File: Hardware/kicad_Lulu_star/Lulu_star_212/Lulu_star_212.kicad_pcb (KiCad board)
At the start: 2 copper layers, 16.7 x 14.9 mm, 8 parts, among them J1 Conn_01x03_Female, P1 Soldering_pad, Q1 Q_NMOS_GSD, T1 Q_NPN_BEC

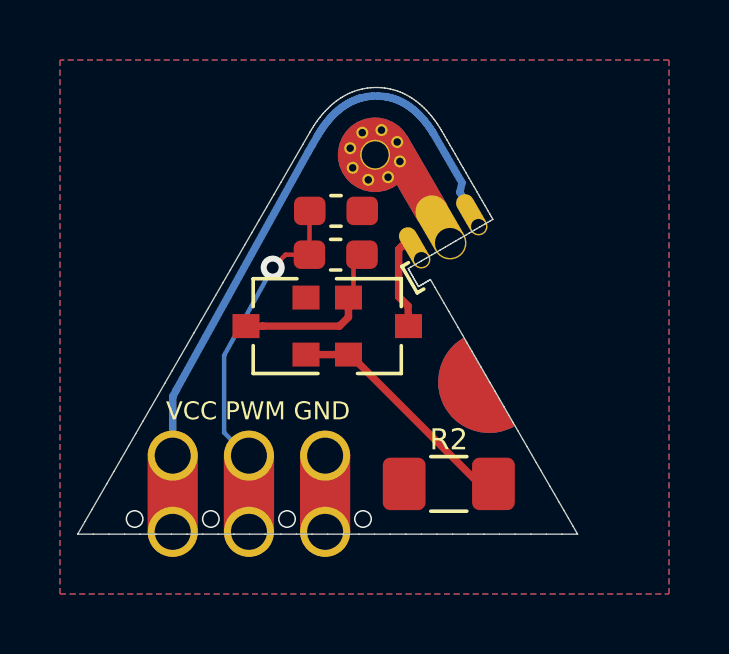
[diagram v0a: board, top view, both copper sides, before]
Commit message: Move down all components of the PCB
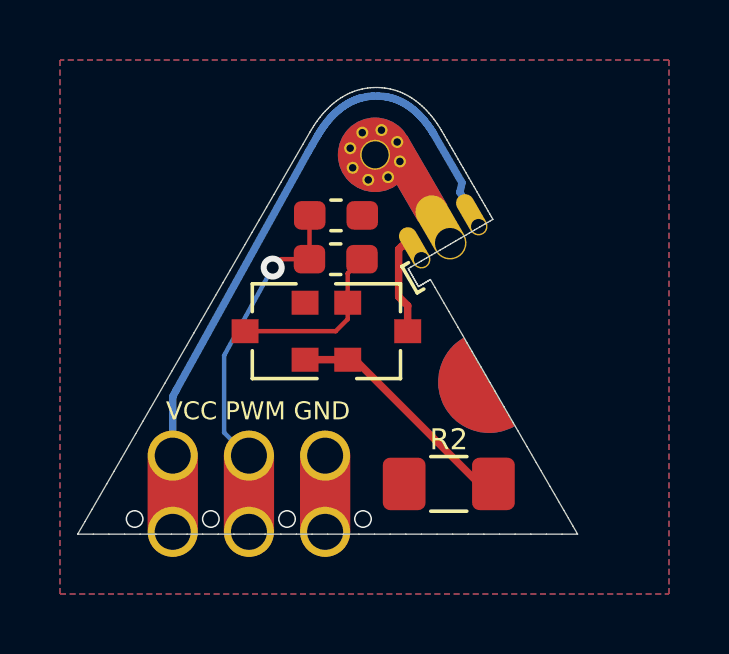
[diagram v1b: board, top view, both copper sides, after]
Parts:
- moved T1 0.17 mm to (68.8, 38.3)
- moved Q1 0.17 mm to (72.2, 38.3)
- moved R1 0.15 mm to (70.8, 35.9)
- moved R3 0.15 mm to (70.8, 34.5)
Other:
- net class Default: clearance 0.15 -> 0.2
- net class POWER: clearance 0.15 -> 0.2
- net class SIG: clearance 0.15 -> 0.2
- rule trace_clearance: 0.15 -> 0.2
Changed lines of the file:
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@@
     (thickness 1)
     (drawings 292)
-    (tracks 97)
+    (tracks 95)
     (zones 0)
     (modules 8)
@@
   (setup
     (last_trace_width 0.25)
-    (trace_clearance 0.15)
+    (trace_clearance 0.2)
     (zone_clearance 0.12)
     (zone_45_only yes)
@@
   (net 6 +3V3)
   (net_class Default "This is the default net class."
-    (clearance 0.15)
+    (clearance 0.2)
     (trace_width 0.25)
     (via_dia 0.8)
@@
   )
   (net_class POWER ""
-    (clearance 0.15)
+    (clearance 0.2)
     (trace_width 0.25)
     (via_dia 0.8)
@@
   )
   (net_class SIG ""
-    (clearance 0.15)
+    (clearance 0.2)
     (trace_width 0.15)
     (via_dia 0.8)
@@
   )
   (module Resistor_SMD:R_0603_1608Metric_Pad1.05x0.95mm_HandSolder (layer F.Cu)
-    (at 70.84 34.33)
+    (at 70.84 34.48)
     (descr "Resistor SMD 0603 (1608 Metric), square (rectangular) end terminal, IPC_7351 nominal with elongated pad for handsoldering. (Body size source: http://www.tortai-tech.com/upload/download/2011102023233369053.pdf), generated with kicad-footprint-generator")
     (tags "resistor handsolder")
@@
       (net 4 /PWM) (zone_connect 1))
     (pad 2 smd roundrect (at 0.875 0) (size 1.05 0.95) (layers F.Cu F.Paste F.Mask) (roundrect_rratio 0.25)
-      (net 2 GND) (zone_connect 1) (thermal_gap 0.3))
+      (net 2 GND) (zone_connect 1) (thermal_gap 0.25))
     (model ${KISYS3DMOD}/Resistor_SMD.3dshapes/R_0603_1608Metric.wrl
       (at (xyz 0 0 0))
@@
   )
   (module Package_TO_SOT_SMD:SOT-23 (layer F.Cu)
-    (at 68.84 38.17 180)
+    (at 68.81 38.34 180)
     (descr "SOT-23, Standard")
     (tags SOT-23)
@@
       (net 3 "Net-(Q1-Pad1)"))
     (pad 2 smd rect (at -1 0.95 180) (size 0.9 0.8) (layers F.Cu F.Paste F.Mask)
-      (net 2 GND) (zone_connect 1) (thermal_gap 0.3))
+      (net 2 GND) (zone_connect 1) (thermal_gap 0.25))
     (pad 1 smd rect (at -1 -0.95 180) (size 0.9 0.8) (layers F.Cu F.Paste F.Mask)
       (net 1 "Net-(Q1-Pad2)"))
@@
   )
   (module Package_TO_SOT_SMD:SOT-23 (layer F.Cu)
-    (at 72.256 38.17)
+    (at 72.23 38.34)
     (descr "SOT-23, Standard")
     (tags SOT-23)
@@
   )
   (module Resistor_SMD:R_0603_1608Metric_Pad1.05x0.95mm_HandSolder (layer F.Cu)
-    (at 70.83 35.79 180)
+    (at 70.83 35.94 180)
     (descr "Resistor SMD 0603 (1608 Metric), square (rectangular) end terminal, IPC_7351 nominal with elongated pad for handsoldering. (Body size source: http://www.tortai-tech.com/upload/download/2011102023233369053.pdf), generated with kicad-footprint-generator")
     (tags "resistor handsolder")
@@
     (fp_line (start -1.6 0.8) (end -1.6 -0.8) (layer F.Fab) (width 0.1))
     (pad 2 smd roundrect (at 1.4875 0 180) (size 1.425 1.75) (layers F.Cu F.Paste F.Mask) (roundrect_rratio 0.175)
-      (net 2 GND) (zone_connect 1) (thermal_gap 0.3))
+      (net 2 GND) (zone_connect 1) (thermal_gap 0.25))
     (pad 1 smd roundrect (at -1.4875 0 180) (size 1.425 1.75) (layers F.Cu F.Paste F.Mask) (roundrect_rratio 0.175439)
       (net 1 "Net-(Q1-Pad2)"))
@@
     (effects (font (size 2 2) (thickness 0.4)) (justify mirror))
   )
-  (segment (start 69.7 39.12) (end 71.256 39.12) (width 0.25) (layer F.Cu) (net 1))
   (segment (start 75.616 43.43) (end 76.0875 43.43) (width 0.25) (layer F.Cu) (net 1))
   (segment (start 71.306 39.12) (end 75.616 43.43) (width 0.25) (layer F.Cu) (net 1))
   (segment (start 71.256 39.12) (end 71.306 39.12) (width 0.25) (layer F.Cu) (net 1))
+  (segment (start 71.23 39.29) (end 69.81 39.29) (width 0.25) (layer F.Cu) (net 1))
   (via (at 71.74 44.6) (size 0.6) (drill 0.5) (layers F.Cu B.Cu) (net 2))
   (via (at 69.208 44.6) (size 0.6) (drill 0.5) (layers F.Cu B.Cu) (net 2))
   (via (at 66.668 44.6) (size 0.6) (drill 0.5) (layers F.Cu B.Cu) (net 2))
   (via (at 64.128 44.6) (size 0.6) (drill 0.5) (layers F.Cu B.Cu) (net 2))
-  (segment (start 70.956 38.17) (end 68.4 38.17) (width 0.25) (layer F.Cu) (net 3))
-  (segment (start 71.256 37.87) (end 70.956 38.17) (width 0.25) (layer F.Cu) (net 3))
-  (segment (start 71.256 37.22) (end 71.256 37.87) (width 0.25) (layer F.Cu) (net 3))
-  (segment (start 68.4 38.17) (end 67.84 38.17) (width 0.25) (layer F.Cu) (net 3))
   (segment (start 71.24 37.204) (end 71.256 37.22) (width 0.15) (layer F.Cu) (net 3))
-  (segment (start 71.425 37.051) (end 71.256 37.22) (width 0.15) (layer F.Cu) (net 3))
-  (segment (start 71.425 35.79) (end 71.425 37.051) (width 0.15) (layer F.Cu) (net 3))
+  (segment (start 71.23 37.39) (end 71.23 36.415) (width 0.15) (layer F.Cu) (net 3))
+  (segment (start 71.23 36.415) (end 71.705 35.94) (width 0.15) (layer F.Cu) (net 3))
+  (segment (start 71.23 37.94) (end 71.23 37.39) (width 0.15) (layer F.Cu) (net 3))
+  (segment (start 70.83 38.34) (end 71.23 37.94) (width 0.15) (layer F.Cu) (net 3))
+  (segment (start 67.81 38.34) (end 70.83 38.34) (width 0.15) (layer F.Cu) (net 3))
   (segment (start 69.955 34.32) (end 69.955 35.79) (width 0.15) (layer F.Cu) (net 4))
-  (segment (start 69.130001 35.820001) (end 68.730002 36.22) (width 0.15) (layer F.Cu) (net 4))
-  (segment (start 69.160002 35.79) (end 69.130001 35.820001) (width 0.15) (layer F.Cu) (net 4))
-  (segment (start 69.675 35.79) (end 69.160002 35.79) (width 0.15) (layer F.Cu) (net 4))
-  (via (at 68.730002 36.22) (size 0.8) (drill 0.4) (layers F.Cu B.Cu) (net 4))
   (segment (start 68.730002 36.22) (end 67.11 39.15) (width 0.15) (layer B.Cu) (net 4))
   (segment (start 67.11 39.15) (end 67.11 41.72) (width 0.15) (layer B.Cu) (net 4))
+  (segment (start 69.010002 35.94) (end 68.730002 36.22) (width 0.15) (layer F.Cu) (net 4))
+  (segment (start 67.11 41.72) (end 67.878 42.488) (width 0.15) (layer B.Cu) (net 4))
+  (segment (start 69.955 35.94) (end 69.010002 35.94) (width 0.15) (layer F.Cu) (net 4))
+  (via (at 68.730002 36.22) (size 0.8) (drill 0.4) (layers F.Cu B.Cu) (net 4))
   (segment (start 67.878 42.488) (end 67.938 42.488) (width 0.15) (layer B.Cu) (net 4))
-  (segment (start 67.11 41.72) (end 67.878 42.488) (width 0.15) (layer B.Cu) (net 4))
   (segment (start 72.93 35.61) (end 73.04 35.5) (width 0.25) (layer F.Cu) (net 5))
   (segment (start 72.93 37.19) (end 72.93 35.61) (width 0.25) (layer F.Cu) (net 5))
-  (segment (start 73.256 38.17) (end 73.24 37.5) (width 0.25) (layer F.Cu) (net 5))
-  (segment (start 73.24 37.5) (end 72.93 37.19) (width 0.25) (layer F.Cu) (net 5))
   (segment (start 73.236671 35.5) (end 73.511976 35.775305) (width 0.25) (layer F.Cu) (net 5))
   (segment (start 73.04 35.5) (end 73.236671 35.5) (width 0.25) (layer F.Cu) (net 5))
+  (segment (start 72.93 37.19) (end 73.23 37.49) (width 0.25) (layer F.Cu) (net 5))
+  (segment (start 73.23 37.49) (end 73.23 38.34) (width 0.25) (layer F.Cu) (net 5))
   (segment (start 65.398 43.758) (end 65.398 42.488) (width 0.25) (layer F.Cu) (net 6))
   (segment (start 74.016659 31.634503) (end 74.058855 31.69999) (width 0.25) (layer B.Cu) (net 6))
